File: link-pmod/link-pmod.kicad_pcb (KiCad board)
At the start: 2 copper layers, 31.8 x 25.4 mm, 5 parts, among them J1 Mini-DIN-8, J2 PMOD, J3 GB

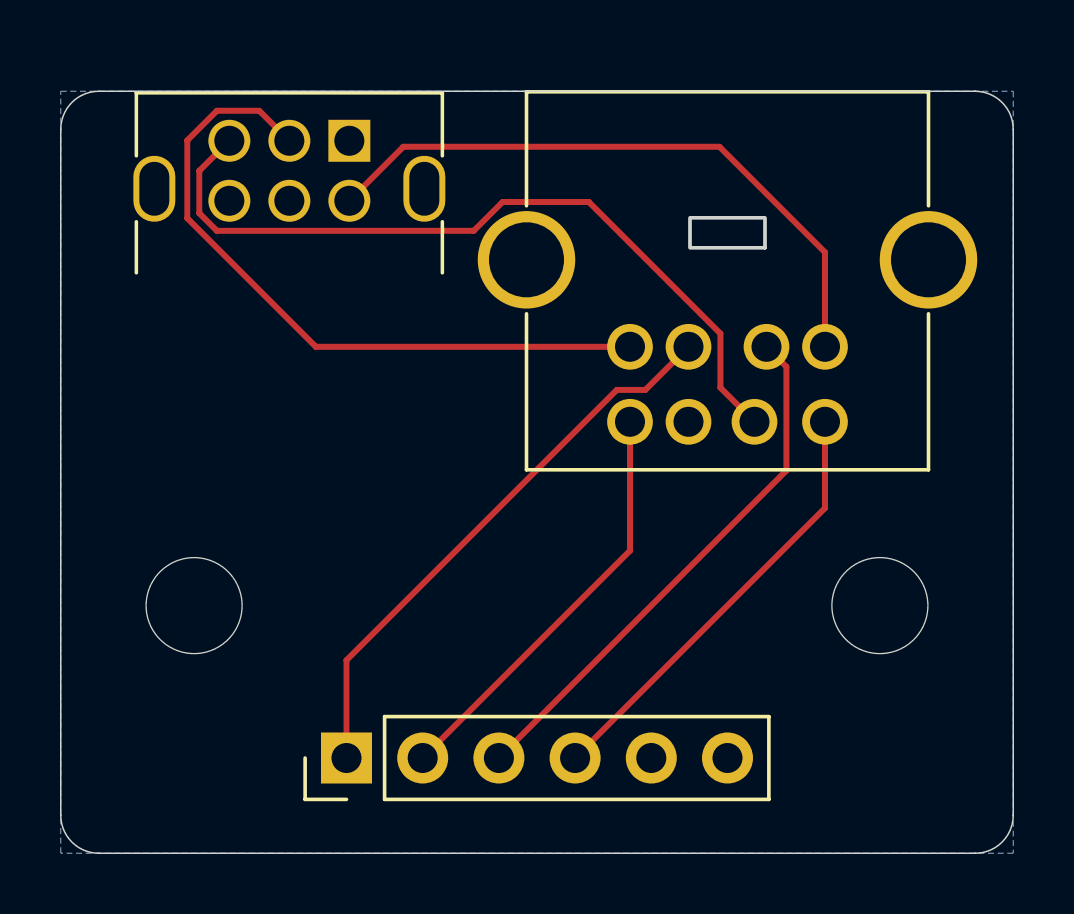
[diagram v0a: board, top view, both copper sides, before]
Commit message: Fix orientation of link-pmod GB link port
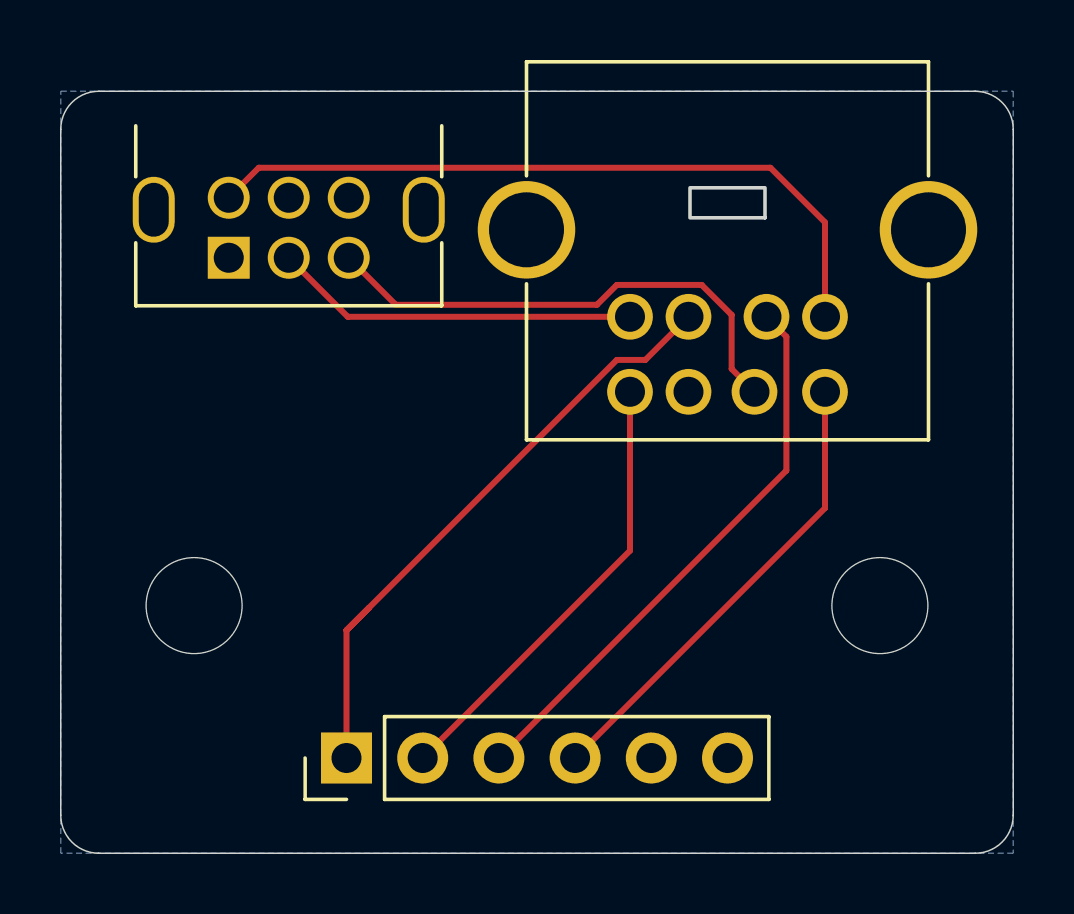
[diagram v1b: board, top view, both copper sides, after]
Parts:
- moved J3 5.60 mm to (94.5, 113.5), turned to 90 degrees
- moved J1 1.00 mm to (111.1, 107.0)
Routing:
- net TX: track 23.4 -> 12.2 mm
- net NMI: track 26.1 -> 17.0 mm
- net RX: track 21.2 -> 24.2 mm
- net PC0: track 19.0 -> 21.0 mm
- net PC3: track 14.7 -> 15.7 mm
- net PC2: track 18.0 -> 19.0 mm
- net PC1: track 14.1 -> 15.1 mm
